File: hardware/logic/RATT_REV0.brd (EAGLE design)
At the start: 109.3 x 76.2 mm, 86 parts, among them J3 F-1X06-SIP-100-40, J4 F-1X07-SIP-100-40, J5 F-1X02-SIP-100-40, Q1 2.5A/30V, Q2 MBT3904DW1T1, Q3 2.5A/30V, Q5 2N7002, Q6 2.5A/30V, U3 MCP73831, U5 AP2112K-3.3V, U6 PCA9539PW

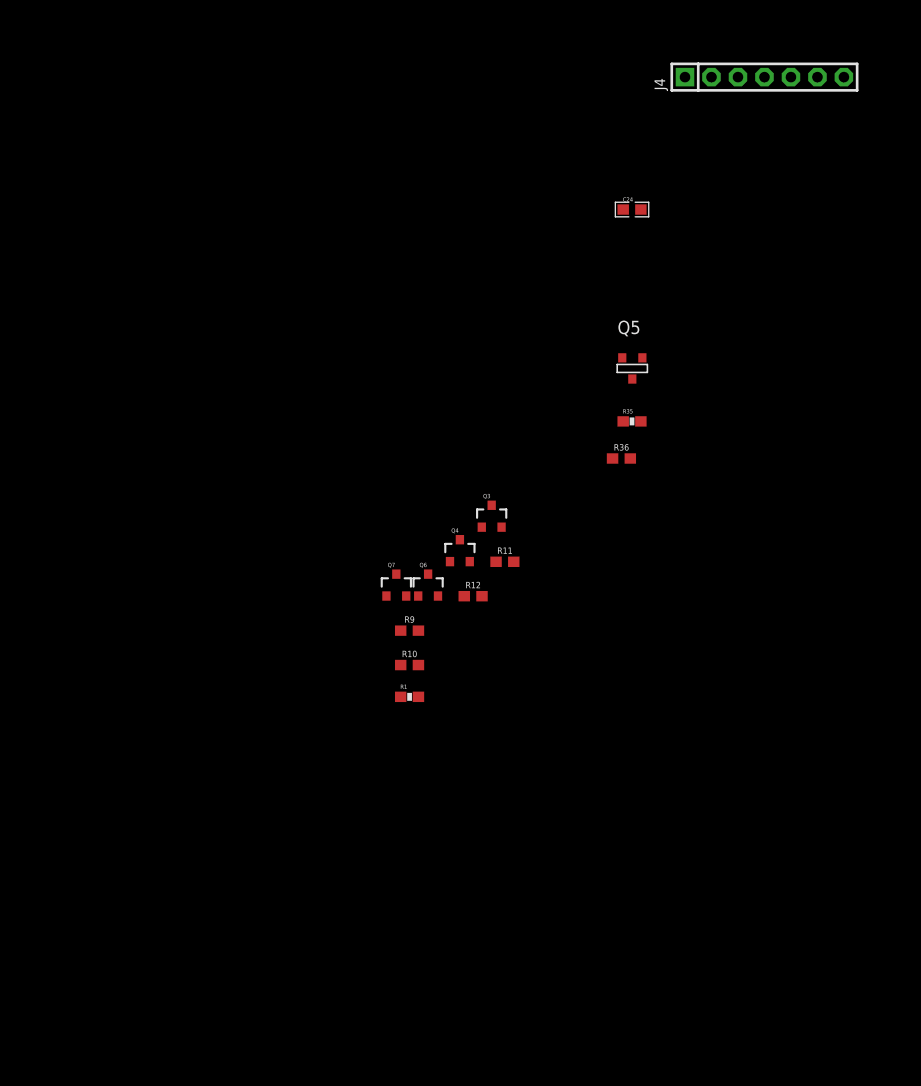
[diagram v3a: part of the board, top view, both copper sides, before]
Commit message: Optos added, cleaning
Added optos to the inputs, cleaned up the schematic a little.
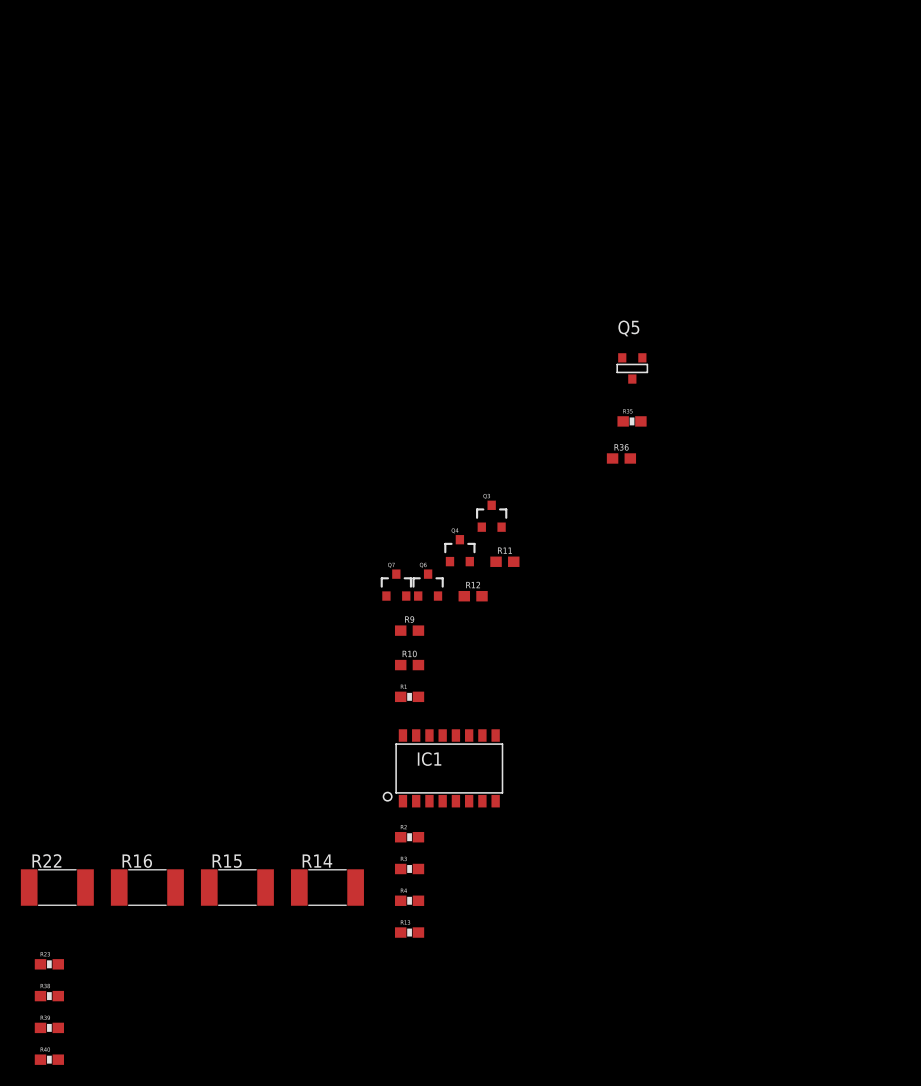
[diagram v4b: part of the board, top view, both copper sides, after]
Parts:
- removed C24: 0.1uF, SparkFun-Capacitors:0603-CAP@1
- removed J4: F-1X07-SIP-100-40, con-headers-jp:SIP-100-07-40
- added IC1: TLP292-4, DURRIDGE-IC:SO-16
- added R13, R2, R3, R4: 10K, SparkFun-Resistors:0603-RES
- added R14, R15, R16, R22: 680R, DURRIDGE-RESISTORS:2512-RES
- added R23, R38, R39, R40: 0R, SparkFun-Passives:0603-RES
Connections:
- removed net JTAG_TCK: J4.6
- removed net JTAG_TDI: J4.5
- removed net JTAG_TDO: J4.7
- removed net JTAG_TMS: J4.4
- new net LED0: U6.17
- new net LED1: U6.18
- new net N$15: IC1.2, R23.1
- new net N$19: IC1.1, R14.2
- new net N$20: IC1.8, R40.1
- new net N$23: IC1.7, R22.2
- new net N$24: IC1.6, R39.1
- new net N$25: IC1.5, R16.2
- new net N$36: IC1.4, R38.1
- new net N$39: IC1.3, R15.2
- new net N$40: R38.2
- new net N$41: R15.1
- new net N$42: R23.2
- new net N$43: R14.1
- new net N$44: R16.1
- new net N$45: R39.2
- new net N$46: R22.1
- new net N$47: R40.2
- net !I/O_IRQ: now also R28.1; no longer R25.1
- net !I/O_RESET: now also R29.1; no longer R30.1
- net +3V3: now also R13.2, R2.2, R3.2, R4.2; no longer C24.1, J4.2
- net GND: now also IC1.11, IC1.13, IC1.15, IC1.9; no longer C24.2, J4.1
- net I2C_SCL: now also R25.1; no longer R29.1
- net I2C_SDA: now also R30.1; no longer R28.1
- net IN0: now also IC1.16, R2.1
- net IN1: now also IC1.14, R3.1
- net IN2: now also IC1.12, R4.1
- net IN3: now also IC1.10, R13.1
- net ~RESET: no longer J4.3

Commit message: All sorts of shit
I/Os are done, connectors, protections, options all added.  Screen updated, library updated, very close to layout ready.
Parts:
- added D10, D2, D5, D6, D7, D8, D9: BAT54S, DURRIDGE-DIODES:SOT-23
- added IC2, IC3, IC4, IC5: CPC1002N, MakeItLabs:CPC1002N
- added J1, J2, J4, J6: (no value), MakeItLabs:HW4-2.0-90D
- added J7, J8: PHOENIX1803484, MakeItLabs:1803484
- added JP1: (no value), pinhead:2X08
- added LED1, LED2: (no value), SparkFun-LED:LED5MM
- added LED3: RED, SparkFun-LED:LED-0603
- added R41, R42: 680R, SparkFun-Resistors:0603-RES
- added R43, R44, R45, R46, R47, R48, R49, R50: 100R, SparkFun-Resistors:0603-RES
- added R51, R52, R53, R54: 680R, SparkFun-Passives:0603-RES
- D3: value RED -> BAT54S; device SparkFun-LED:LED-0603 -> DURRIDGE-DIODES:SOT-23
- LCD1: device MakeIt_Labs:1.8TFT_ADA -> MakeItLabs:1.8TFT_ADA
- LCD3: device MakeIt_Labs:1.8TFT_CHI_2.0 -> MakeItLabs:1.8TFT_CHI_2.0
- moved D3 350.5 mm to (-170.9, -370.8), turned to 270 degrees
- moved IC1 272.0 mm to (-297.4, -451.4), turned to 180 degrees
- moved R3 268.3 mm to (-294.6, -460.2)
- moved R2 267.1 mm to (-291.8, -457.2)
- moved R13 265.3 mm to (-299.7, -460.2)
- moved R4 264.1 mm to (-297.2, -457.2)
- moved R14 239.6 mm to (-284.0, -439.2), turned to 270 degrees
- moved R15 239.3 mm to (-291.8, -439.2), turned to 270 degrees
- moved R16 238.8 mm to (-299.2, -439.2), turned to 270 degrees
- moved R22 238.3 mm to (-306.8, -439.2), turned to 270 degrees
- moved R40 224.6 mm to (-310.6, -438.9), turned to 270 degrees
- moved R39 224.2 mm to (-303.0, -439.2), turned to 270 degrees
- moved R23 224.0 mm to (-288.0, -439.2), turned to 270 degrees
- moved R38 223.9 mm to (-295.4, -439.2), turned to 270 degrees
- moved LCD3 22.9 mm to (40.6, 37.6), turned to 270 degrees
- renumbered U$1 to U1, U3 to IC13, U6 to IC16
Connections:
- new net N$48: LED1.A, R41.1
- new net N$49: LED2.A, R42.1
- new net N$50: J2.1, R43.2
- new net N$51: J2.2, R44.2
- new net N$52: J1.1, R45.2
- new net N$53: J1.2, R46.2
- new net N$54: J4.1, R47.2
- new net N$55: J4.2, R48.2
- new net N$56: J6.1, R49.2
- new net N$57: J6.2, R50.2
- new net N$58: IC2.1, R51.1
- new net N$59: IC2.4, J8.1
- new net N$60: IC2.3, J8.2
- new net N$61: IC3.1, R52.1
- new net N$62: IC3.4, J8.3
- new net N$63: IC3.3, J8.4
- new net N$64: IC4.4, J8.5
- new net N$65: IC4.3, J8.6
- new net N$66: IC5.4, J8.7
- new net N$67: IC5.3, J8.8
- new net N$68: IC4.1, R53.1
- new net N$69: IC5.1, R54.1
- net +3V3: now also JP1.3, R41.2, R42.2
- net +5V: now also D10.2, D2.2, D3.2, D5.2, D6.2, D7.2, D8.2, D9.2, J1.3, J2.3, J4.3, J6.3, JP1.5
- net GND: now also D10.1, D2.1, D3.1, D5.1, D6.1, D7.1, D8.1, D9.1, IC2.2, IC3.2, IC4.2, IC5.2, J1.4, J2.4, J4.4, J6.4, JP1.1, JP1.7, LED3.C; no longer D3.C
- net I2C_SCL: now also JP1.9
- net I2C_SDA: now also JP1.11
- net IN0: now also D6.3, JP1.2, R45.1
- net IN1: now also D5.3, JP1.4, R46.1
- net IN2: now also D3.3, JP1.6, R43.1
- net IN3: now also D2.3, JP1.8, R44.1
- net LED0: now also LED1.K
- net LED1: now also LED2.K
- net N$11: now also LED3.A; no longer D3.A
- net N$40: now also J7.4
- net N$41: now also J7.3
- net N$42: now also J7.2
- net N$43: now also J7.1
- net N$44: now also J7.5
- net N$45: now also J7.6
- net N$46: now also J7.7
- net N$47: now also J7.8
- net OUT0: now also D8.3, JP1.10, R47.1, R51.2
- net OUT1: now also D7.3, JP1.12, R48.1, R52.2
- net OUT2: now also D10.3, JP1.14, R49.1, R53.2
- net OUT3: now also D9.3, JP1.16, R50.1, R54.2
- net RFID_RX: now also JP1.15
- net RFID_TX: now also JP1.13

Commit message: Stuff we done
stuff I did Thursday and didn't commit
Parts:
- moved IC5 541.6 mm to (105.7, -22.4)
- moved JP1 541.6 mm to (88.4, -42.7)
- moved R54 541.6 mm to (104.1, -28.4)
- moved IC1 541.6 mm to (49.0, -35.1)
- moved IC2 541.6 mm to (82.8, -22.6)
- moved IC3 541.6 mm to (90.7, -22.6)
- moved IC4 541.6 mm to (98.0, -22.6)
- moved J7 541.6 mm to (49.0, -14.5)
- moved J8 541.6 mm to (94.5, -13.7)
- moved R13 541.6 mm to (46.7, -43.9)
- moved R14 541.6 mm to (62.5, -22.9)
- moved R15 541.6 mm to (54.6, -22.9)
- moved R16 541.6 mm to (47.2, -22.9)
- moved R2 541.6 mm to (54.6, -40.9)
- moved R22 541.6 mm to (39.6, -22.9)
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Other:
- board size 109.3 x 76.2 mm -> 190.5 x 76.2 mm

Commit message: saturday ratt
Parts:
- removed J5: F-1X02-SIP-100-40, con-headers-jp:SIP-100-02-40
- removed LCD1: 1.8TFT_ADA, MakeItLabs:1.8TFT_ADA
- J1, J2, J4, J6: value (none) -> 4P-2.0; device MakeItLabs:HW4-2.0-90D -> MakeItLabs:HW4-2.0
- moved F1 129.8 mm to (-10.4, 71.1), turned to 0 degrees
- moved IC16 129.7 mm to (96.5, 39.6), turned to 180 degrees
- moved LED2 113.5 mm to (5.84, 19.6)
- moved LED1 113.1 mm to (6.10, 11.4)
- moved J1 112.9 mm to (100.3, -10.7)
- moved J2 110.3 mm to (111.3, -11.4)
- moved R40 107.2 mm to (127.5, 33.0), turned to 0 degrees
- moved R22 101.8 mm to (127.3, 29.0), turned to 180 degrees
- moved R39 97.2 mm to (127.8, 25.4), turned to 0 degrees
- moved JP2 95.7 mm to (9.91, 67.1), turned to 90 degrees
- moved R13 94.5 mm to (106.2, 29.5), turned to 270 degrees
- moved J7 92.0 mm to (134.6, 19.3), turned to 90 degrees
- moved R16 91.4 mm to (127.3, 21.3), turned to 180 degrees
- moved R54 87.9 mm to (104.9, 59.4), turned to 180 degrees
- moved R4 87.0 mm to (105.7, 25.4), turned to 90 degrees
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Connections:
- removed net N$50: J2.1, R43.2
- removed net N$51: J2.2, R44.2
- removed net N$52: J1.1, R45.2
- removed net N$53: J1.2, R46.2
- removed net N$54: J4.1, R47.2
- removed net N$55: J4.2, R48.2
- removed net N$56: J6.1, R49.2
- removed net N$57: J6.2, R50.2
- removed net N$67: IC5.3, J8.8
- removed net RFID_W0: J3.5
- removed net RFID_W1: J3.6
- new net IN0P: J1.1, JP1.2, R45.2
- new net IN1P: J1.2, JP1.4, R46.2
- new net IN2P: J2.1, JP1.6, R43.2
- new net IN3P: J2.2, JP1.8, R44.2
- new net OUT0P: J4.1, JP1.10, R47.2
- new net OUT1P: J4.2, JP1.12, R48.2
- new net OUT2P: J6.1, JP1.14, R49.2
- new net OUT3P: J6.2, JP1.16, R50.2
- net +3V3: now also J3.3; no longer J3.1
- net 5V_RFID_TX: now also J3.5; no longer J5.2
- net GND: now also J3.1; no longer J3.2
- net IN0: no longer JP1.2
- net IN1: no longer JP1.4
- net IN2: no longer JP1.6
- net IN3: no longer JP1.8
- net N$26: no longer LCD1.2
- net N$27: no longer LCD1.3
- net N$28: no longer LCD1.4
- net N$29: no longer LCD1.6
- net N$3: no longer LCD1.1
- net N$30: no longer LCD1.7
- net N$31: no longer LCD1.8
- net N$32: now also IC2.3, J8.1; no longer LCD1.9, SJ10.1
- net N$33: no longer LCD1.10
- net N$59: now also J8.2; no longer J8.1
- net N$60: now also IC5.3, J8.7; no longer IC2.3, J8.2
- net N$62: now also IC5.4, J8.8; no longer IC3.4, J8.3
- net N$63: now also IC4.3, J8.5; no longer IC3.3, J8.4
- net N$64: now also J8.6; no longer J8.5
- net N$65: now also IC3.3, J8.3; no longer IC4.3, J8.6
- net N$66: now also IC3.4, J8.4; no longer IC5.4, J8.7
- net OUT0: no longer JP1.10
- net OUT1: no longer JP1.12
- net OUT2: no longer JP1.14
- net OUT3: no longer JP1.16
- net RFID_RX: now also J3.6; no longer J3.4
- net RFID_TX: no longer J3.3
- net V_USB: now also J3.2; no longer J5.1
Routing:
- net N$6: track 7.88 -> 87.3 mm
- net N$7: track 7.98 -> 81.7 mm
- net VUSB-RAW: track 2.58 -> 0.00 mm
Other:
- board size 190.5 x 76.2 mm -> 194.3 x 76.2 mm
- board text removed: "RFID Connection"

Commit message: psuedo-routing
psuedo-routing to figure out final routing plan
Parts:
- removed SJ10: JUMPER-PAD-2-NC_BY_TRACE, SparkFun-Passives:PAD-JUMPER-2-NC_BY_TRACE_YES_SILK
- moved R26 121.9 mm to (101.3, 38.6), turned to 90 degrees
- moved R27 110.4 mm to (91.4, 41.4), turned to 270 degrees
- moved R25 90.2 mm to (64.3, 41.4), turned to 270 degrees
- moved R35 81.6 mm to (28.2, 68.8), turned to 270 degrees
- moved R28 80.8 mm to (62.0, 46.0)
- moved R30 79.1 mm to (65.8, 46.0)
- moved R29 72.3 mm to (56.6, 46.2)
- moved Q5 70.3 mm to (31.2, 62.5), turned to 90 degrees
- moved SJ9 49.8 mm to (51.8, 59.3), turned to 270 degrees
- moved SJ8 49.6 mm to (54.4, 59.2), turned to 270 degrees
- moved SJ6 46.6 mm to (56.7, 59.2), turned to 270 degrees
- moved SJ5 43.9 mm to (59.7, 64.3), turned to 90 degrees
- moved SJ7 42.7 mm to (49.3, 59.8), turned to 270 degrees
- moved SJ11 33.7 mm to (43.1, 59.2), turned to 0 degrees
- moved JP1 31.7 mm to (97.8, 26.4)
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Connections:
- net 3V3@2 renamed 3V3
- removed net GND@3: U1.25, U1.39, U1.9
- removed net GND@6: U1.14, U1.20, U1.30, U1.34, U1.6
- net GND: now also U1.14, U1.20, U1.25, U1.30, U1.34, U1.39, U1.6, U1.9
- net LCD_MISO: no longer SJ10.2
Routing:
- net I2S_BCK: track 4.35 -> 75.5 mm
- net LCD_RESET: track 0.00 -> 33.6 mm
- net 3V3: track 0.00 -> 22.2 mm
- net LCD_SCK: track 0.00 -> 17.6 mm
- net LCD_MOSI: track 0.00 -> 15.0 mm
- net OUT3: track 0.00 -> 14.3 mm
- net LCD_CS: track 0.00 -> 13.8 mm
- net !I/O_RESET: track 0.00 -> 13.5 mm
- net I2C_SCL: track 0.00 -> 13.0 mm
- net RFID_RX: track 0.00 -> 12.6 mm
- net LCD_D/C: track 0.00 -> 12.5 mm
- net I2S_DOUT: track 6.12 -> 18.3 mm
- net OUT2: track 0.00 -> 11.6 mm
- net !SHUTDOWN: track 0.00 -> 11.2 mm
- net !BUTTON0: track 0.00 -> 10.9 mm
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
